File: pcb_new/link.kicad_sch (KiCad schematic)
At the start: 94 parts, among them J1 STLINK-V3MINIE, J11 68021-204HLF, J12 68021-204HLF, J13 68021-204HLF, J15 68021-204HLF, J16 68021-204HLF, J17 68021-204HLF, J18 68021-204HLF, SW1 TL6400AF160QJ, U1 STM32F479VGT6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

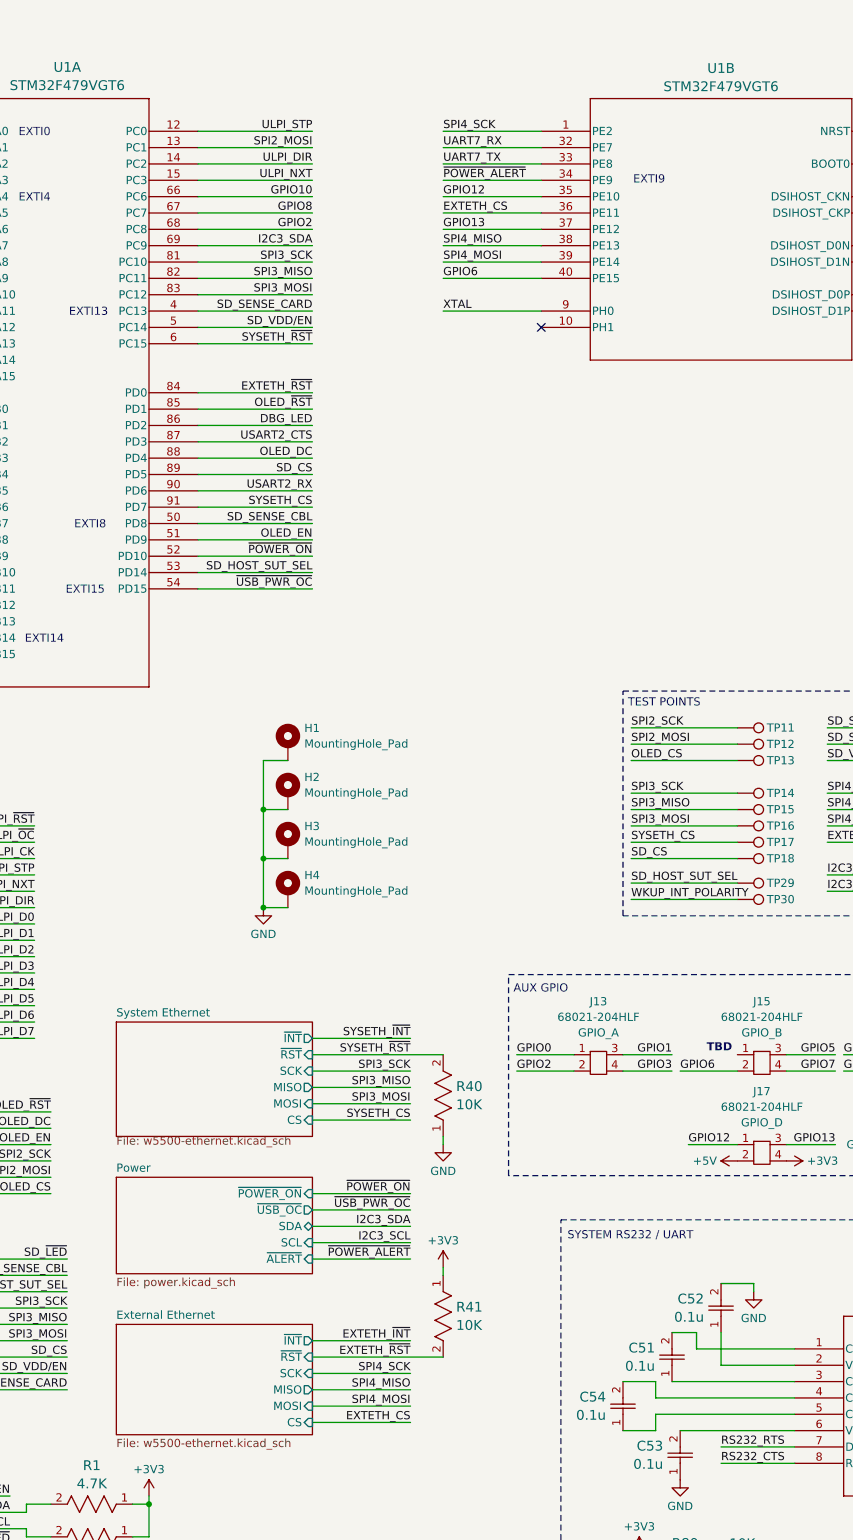
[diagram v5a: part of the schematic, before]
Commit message: separate VBUS/PSU control lines (ref #89) and pull up VBUS enable (ref #68)
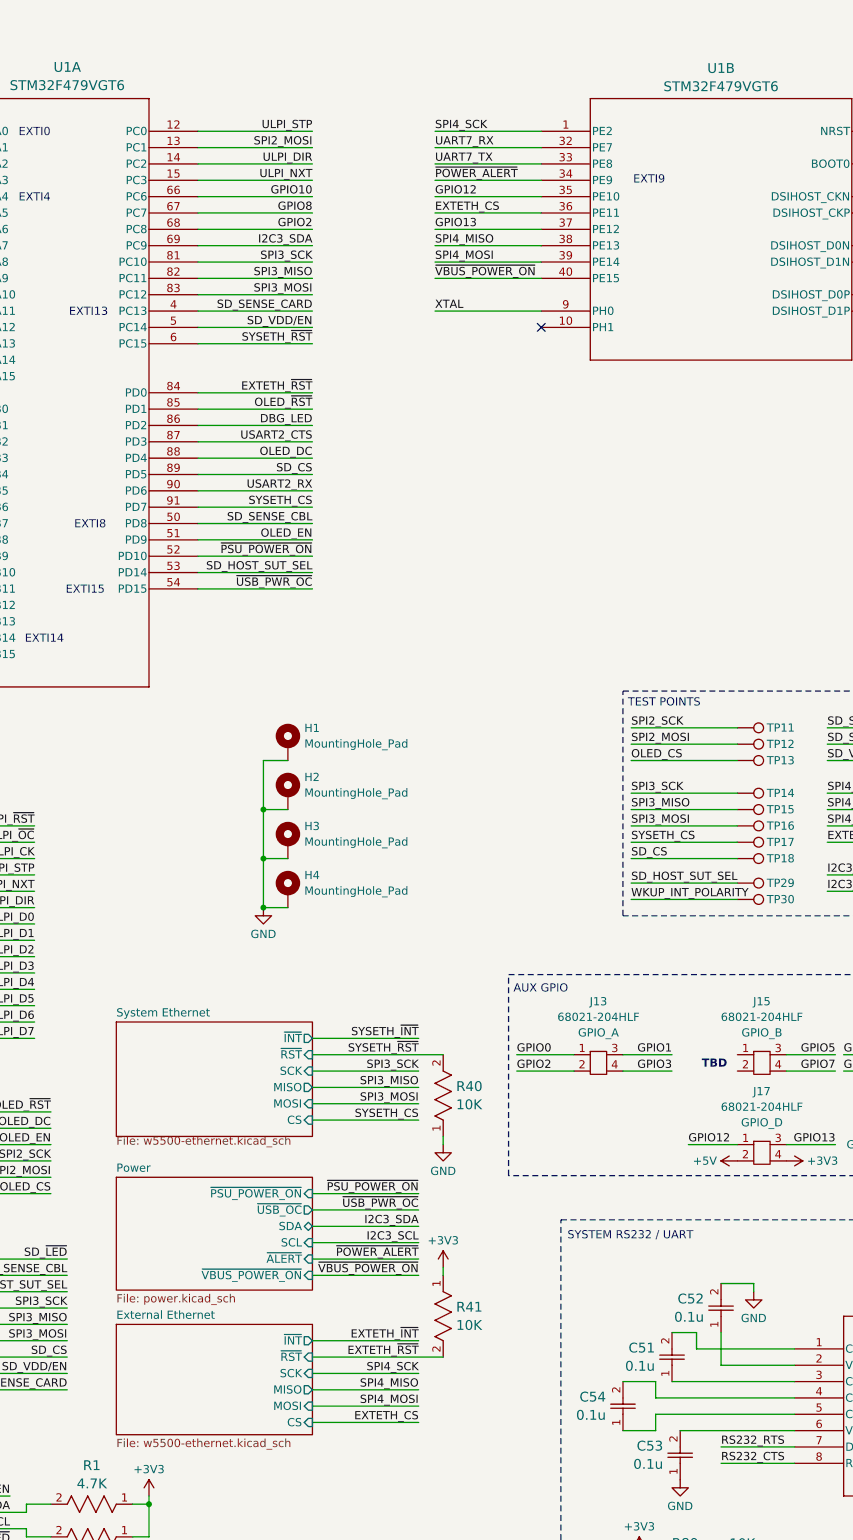
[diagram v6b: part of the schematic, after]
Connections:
- net GPIO6: no longer names the net of J15.2
- net GPIO6: no longer U1.40 (PE15)
- net ~{POWER_ON} renamed ~{PSU_POWER_ON}
- new net ~{VBUS_POWER_ON}: U1.40 (PE15)
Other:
- sheet Power ports: added ~{PSU_POWER_ON}, ~{VBUS_POWER_ON}; removed ~{POWER_ON}

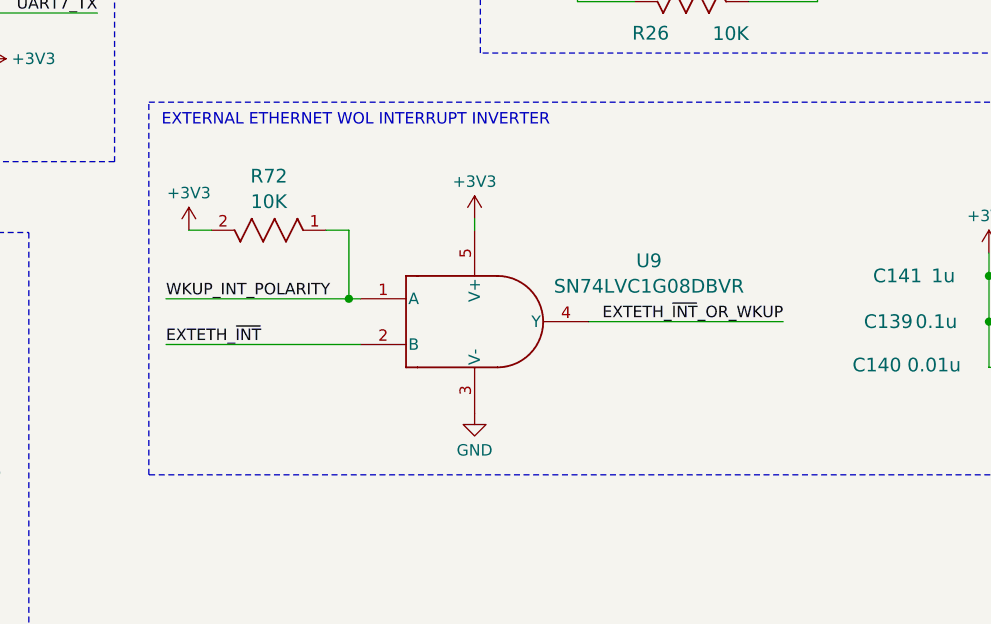
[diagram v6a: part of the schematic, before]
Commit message: replace WOL AND gate with XOR gate (ref #65)
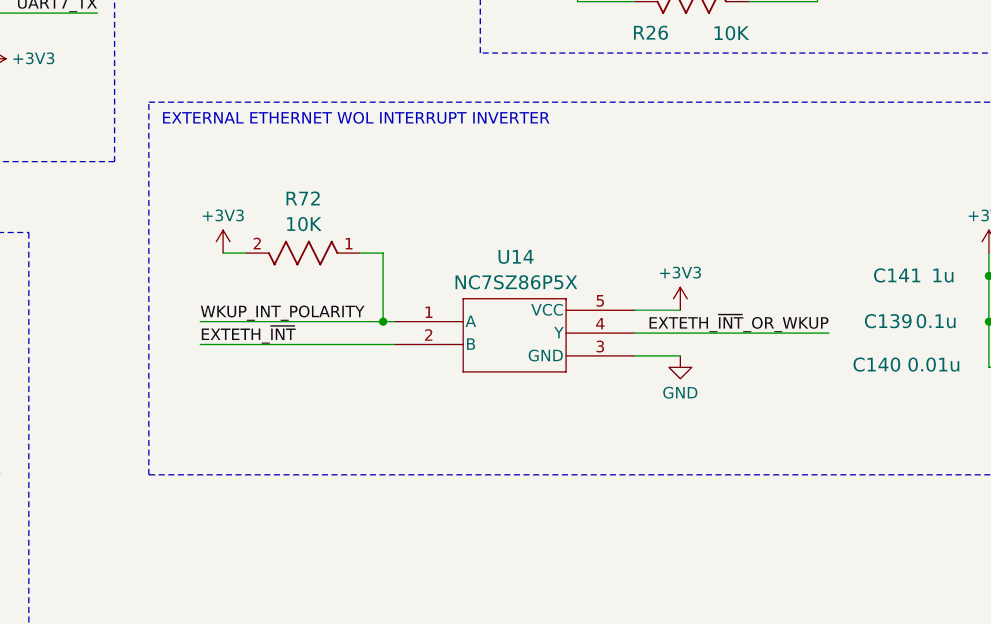
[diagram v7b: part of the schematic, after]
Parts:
- removed U9: SN74LVC1G08DBVR, OroLink:DBV0005A_N, symbol OroLink:SN74LVC1G08DBVR
- added U14: NC7SZ86P5X, OroLink:SC-88A-5_1P35X2P2_ONS, symbol OroLink:NC7SZ86P5X
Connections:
- net +3V3: now also U14.5 (VCC)
- net EXTETH_~{INT}: now also U14.2 (B)
- net EXTETH_~{INT}_OR_WKUP: now also U14.4 (Y)
- net GND: now also U14.3 (GND)
- net WKUP_INT_POLARITY: now also U14.1 (A)
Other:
- moved on the sheet: R72

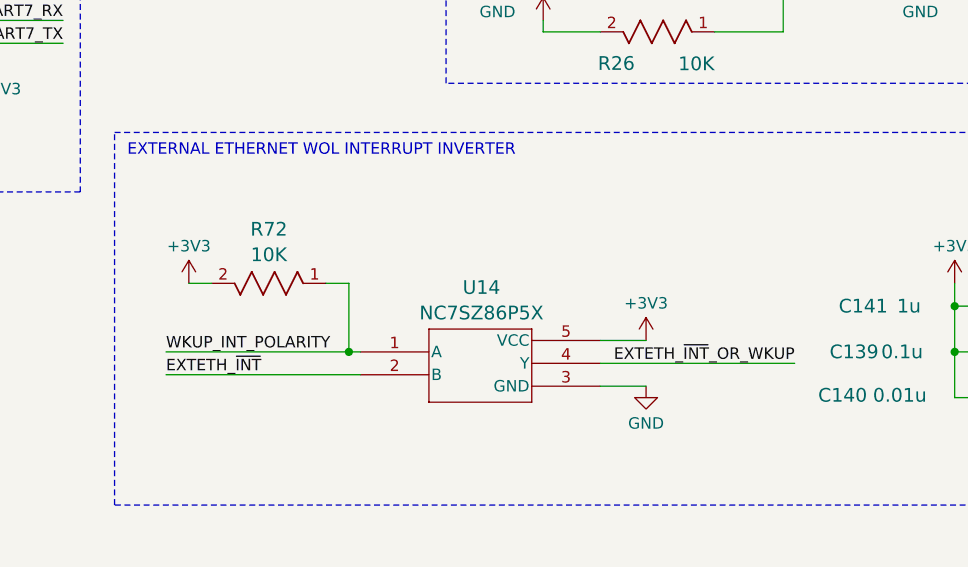
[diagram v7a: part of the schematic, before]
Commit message: pull up `EXTETH_~{INT}_OR_WKUP (ref #66)
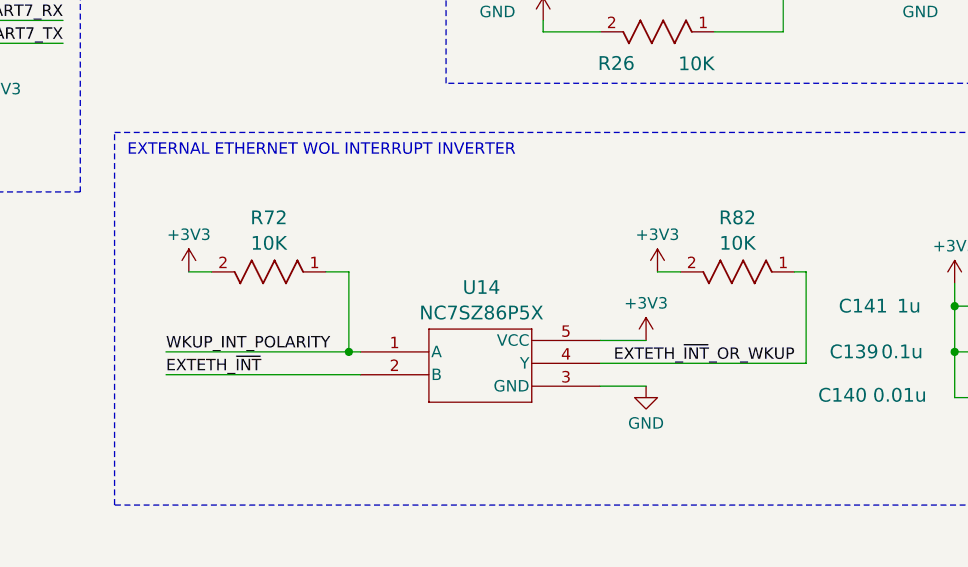
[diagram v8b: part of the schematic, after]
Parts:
- added R82: 10K, OroLink:STA_RMCF0402_STP, symbol OroLink:RMCF0402FT10K0
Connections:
- net +3V3: now also R82.2
- net EXTETH_~{INT}_OR_WKUP: now also R82.1
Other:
- moved on the sheet: R72
